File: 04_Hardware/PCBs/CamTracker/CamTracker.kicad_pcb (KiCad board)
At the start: 6 copper layers, 126.6 x 49.2 mm, 401 parts, among them IC1 W25Q128JVSIM, IC2 AP7361E-33FGE-7, IC3 AP7361E-33FGE-7, J1 PJ-059A, J10 1909763-1, J11 22-28-4034, J12 22-28-4034, J13 2336582-1, J15 1909763-1, J16 1909763-1, J17 1909763-1, J18 2201778-1, J19 2174507-2, J2 67996-100HLF, J21 67996-100HLF, J27 53047-0210, J28 Bus_M.2_Socket_M, J3 67996-100HLF, J5 22-28-4034, J6 2345986-1, J7 22-28-4044, J8 HX JN1.27-2X10 TP H4.9, J9 HX JN1.27-2X10 TP H4.9, M701 M.2 Solder Nut, Q1 BC817-40,215, Q10 BC817-40,215, Q11 BC817-40,215, Q2 BC817-40,215, Q3 BC817-40,215, Q4 BC817-40,215, Q5 BC817-40,215, Q6 BC817-40,215, Q7 BC817-40,215, Q9 BC817-40,215, U1 SC206EEMDA-G51-UGNDA, U10 SGM804, U11 ST4SI2M0020TPIFW, U12 RP2040, U13 PAM8302AASCR, U14 ASM2362, U15 AP61100Z6-7, U2 AP64502QSP-13, U3 AP7335-WG-7, U6 AP61300Z6-7, U7 PI3USB4000DZUAEX, U9 PI3USB4000DZUAEX, Y1 ABM8-272-T3, Y2 25MHz

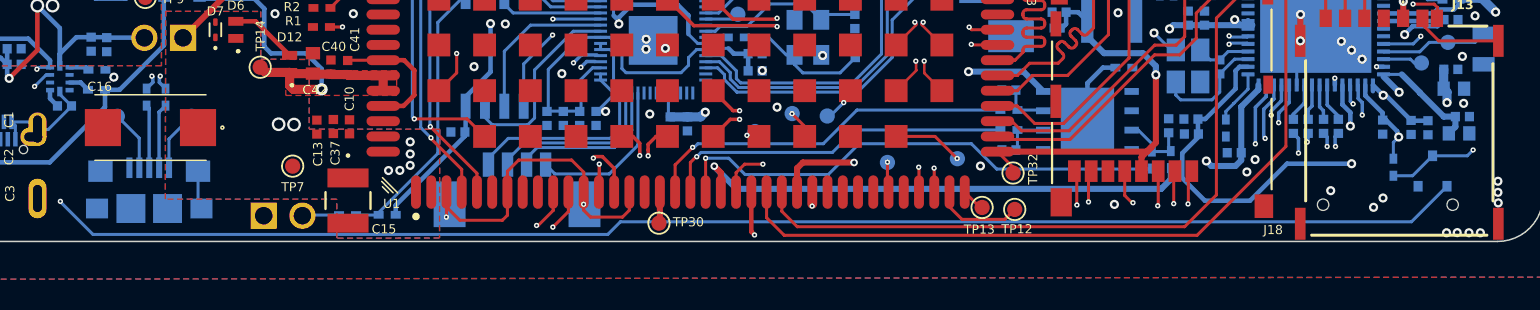
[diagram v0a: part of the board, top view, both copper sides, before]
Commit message: feat(PCB): Added GPIO IN to SC206E from the MCU
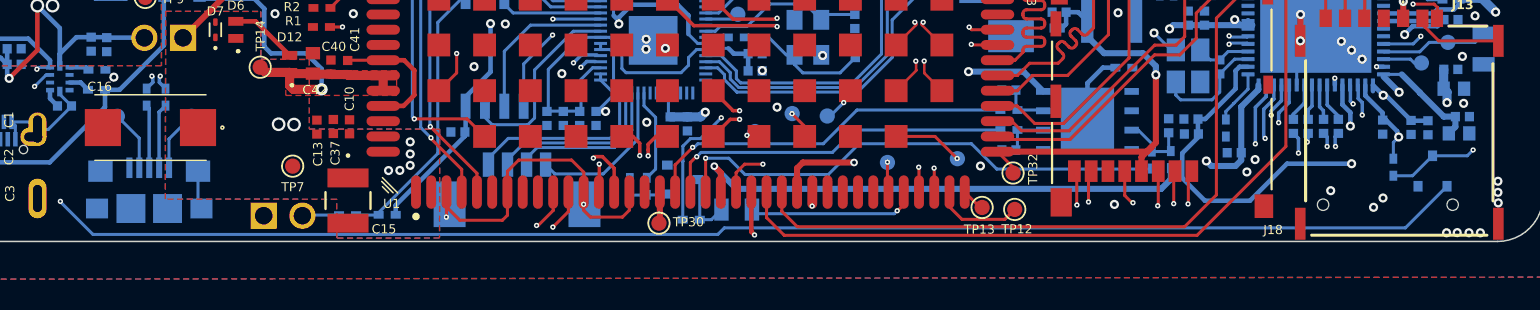
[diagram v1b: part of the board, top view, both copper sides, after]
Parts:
- added Q8: BC817-40,215, 000MCLib:BC81740215, B.Cu at (139.7, 104.2)
- added R28: 10K, 000MCLib:RC0402N_YAG, B.Cu at (137.3, 104.6)
- added R47: 10K, 000MCLib:RC0402N_YAG, B.Cu at (136.2, 104.7)
- added R48: 10K, 000MCLib:RC0402N_YAG, B.Cu at (140.2, 106.8)
- added R50: 0R, 000MCLib:RESC2012X50N, B.Cu at (143.2, 106.2)
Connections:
- U1 pad 33: unconnected-(U1D-GPIO_28-Pad33) -> GPIO28_MCU_IN
- U12 pad 37: unconnected-(U12-GPIO25-Pad37) -> /MCU/MCU_OUT
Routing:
- net LDO15A_1V8: track 215.2 -> 263.2 mm, vias 6 -> 7
- net GPIO28_MCU_IN: track 0.00 -> 11.1 mm, vias 0 -> 1
- net /MCU/MCU_OUT: track 0.00 -> 6.13 mm
- net Net-(Q8-C): track 0.00 -> 4.39 mm
- net Net-(Q8-B): track 0.00 -> 2.49 mm
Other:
- board text added: "5~12VDC"
- board text removed: "5~16VDC"
